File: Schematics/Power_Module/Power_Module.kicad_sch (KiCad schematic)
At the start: 34 parts, among them J1 Screw_Terminal_01x02, J2 Screw_Terminal_01x02, J3 Screw_Terminal_01x02, J4 Screw_Terminal_01x02, J5 Stack Male Edge Connector, Q1 PMOS, Q2 PMOS, U1 LMR51430XDDCR, U2 LMR51430XDDCR, U3 LMR51430XDDCR

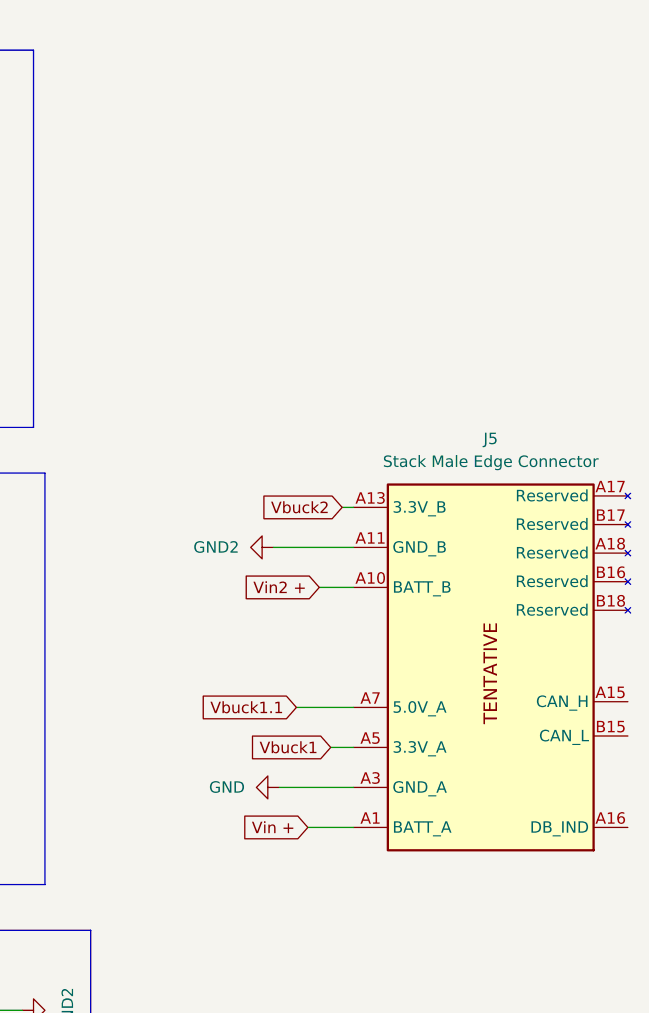
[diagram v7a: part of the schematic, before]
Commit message: Fixed libraries and added updated edge connector
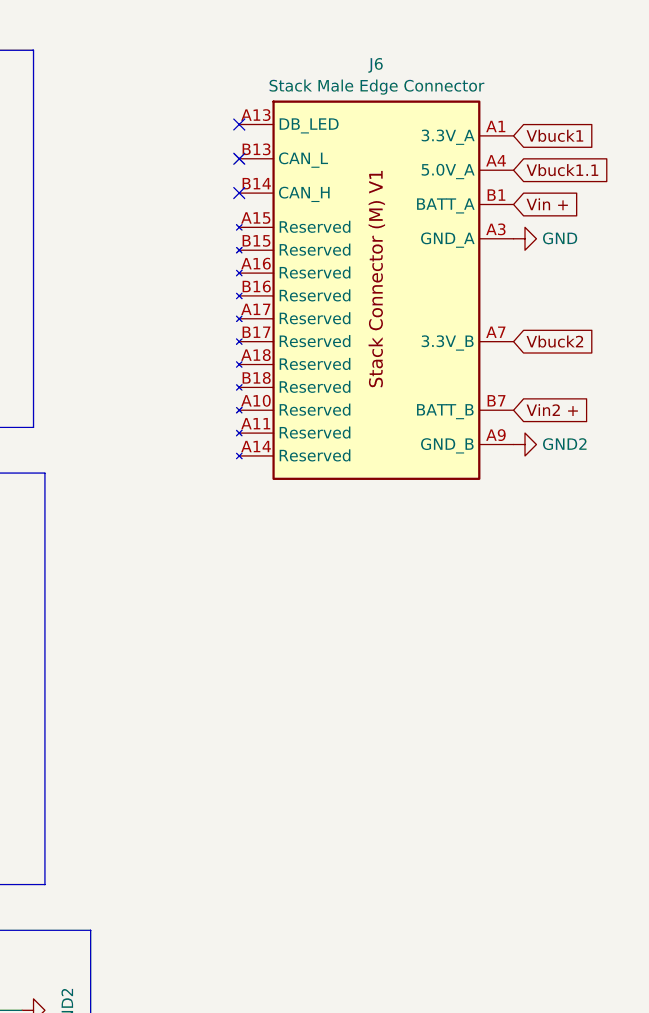
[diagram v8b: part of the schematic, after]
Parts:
- removed J5: Stack Male Edge Connector, Connector_PCBEdge:BUS_PCIexpress_x1, symbol EdgeConnector:Stack Male Edge Connector
- added J6: Stack Male Edge Connector, Connector_PCBEdge:BUS_PCIexpress_x1, symbol EdgeConnector:Stack Male Edge Connector
- U2: footprint footprints:SOT-23-THIN-6_DDC_TEX -> Package_TO_SOT_SMD:SOT-23-6_Handsoldering
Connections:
- net GND: now also J6.A3 (GND_A), J6.A6 (GND_A), J6.B4 (GND_A), J6.B5 (GND_A), J6.B6 (GND_A)
- net GND2: now also J6.A12 (GND_B), J6.A9 (GND_B), J6.B10 (GND_B), J6.B11 (GND_B), J6.B12 (GND_B)
- net Vbuck1: now also J6.A1 (3.3V_A), J6.A2 (3.3V_A)
- net Vbuck2: now also J6.A7 (3.3V_B), J6.A8 (3.3V_B)
- net Vin +: now also J6.B1 (BATT_A), J6.B2 (BATT_A), J6.B3 (BATT_A)
- net Vin 2+: now also J6.B7 (BATT_B), J6.B8 (BATT_B), J6.B9 (BATT_B)
- net Vbuck1.1 renamed 5.0V_A
- net 5.0V_A: now also J6.A4 (5.0V_A), J6.A5 (5.0V_A)
- no-connect marks 0 -> 3
